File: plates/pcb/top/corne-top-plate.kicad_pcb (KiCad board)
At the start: 2 copper layers, 132.9 x 91.4 mm, 28 parts, among them SW2 KEY_SWITCH

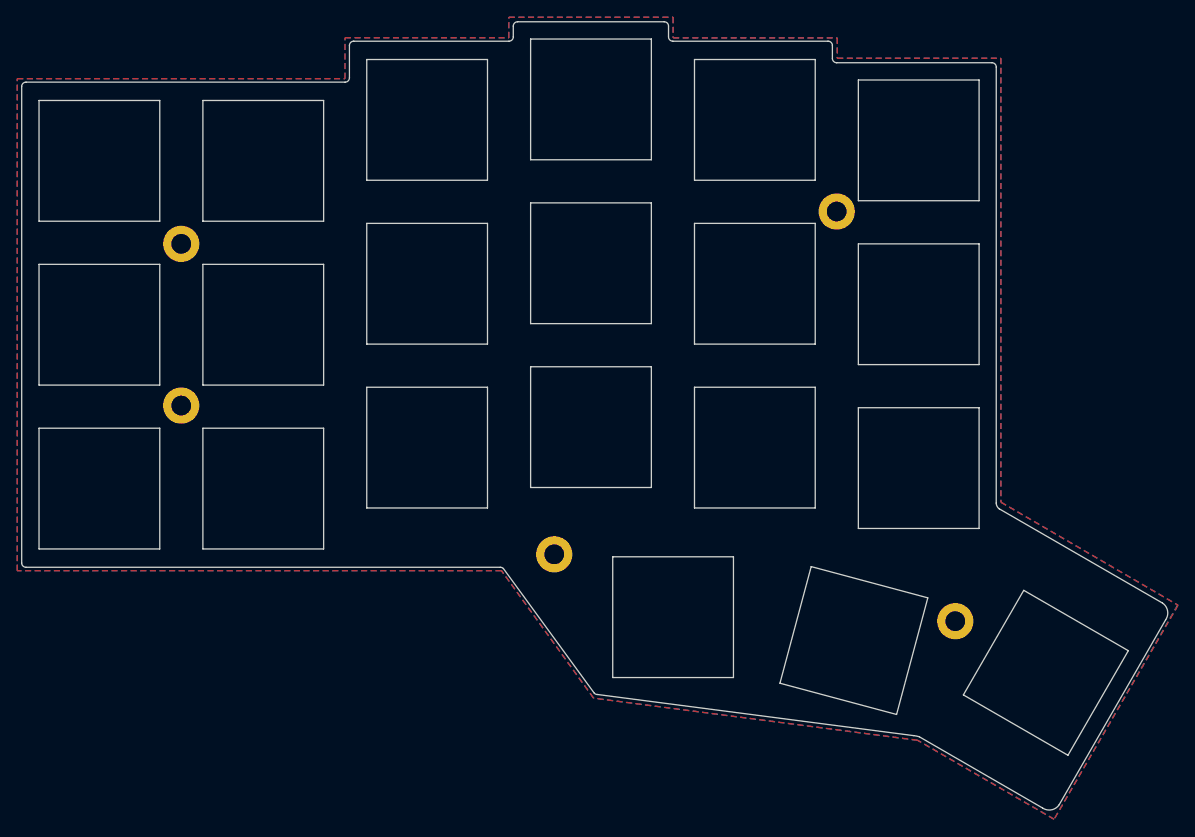
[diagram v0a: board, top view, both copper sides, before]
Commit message: Added light ice trackball inital design.
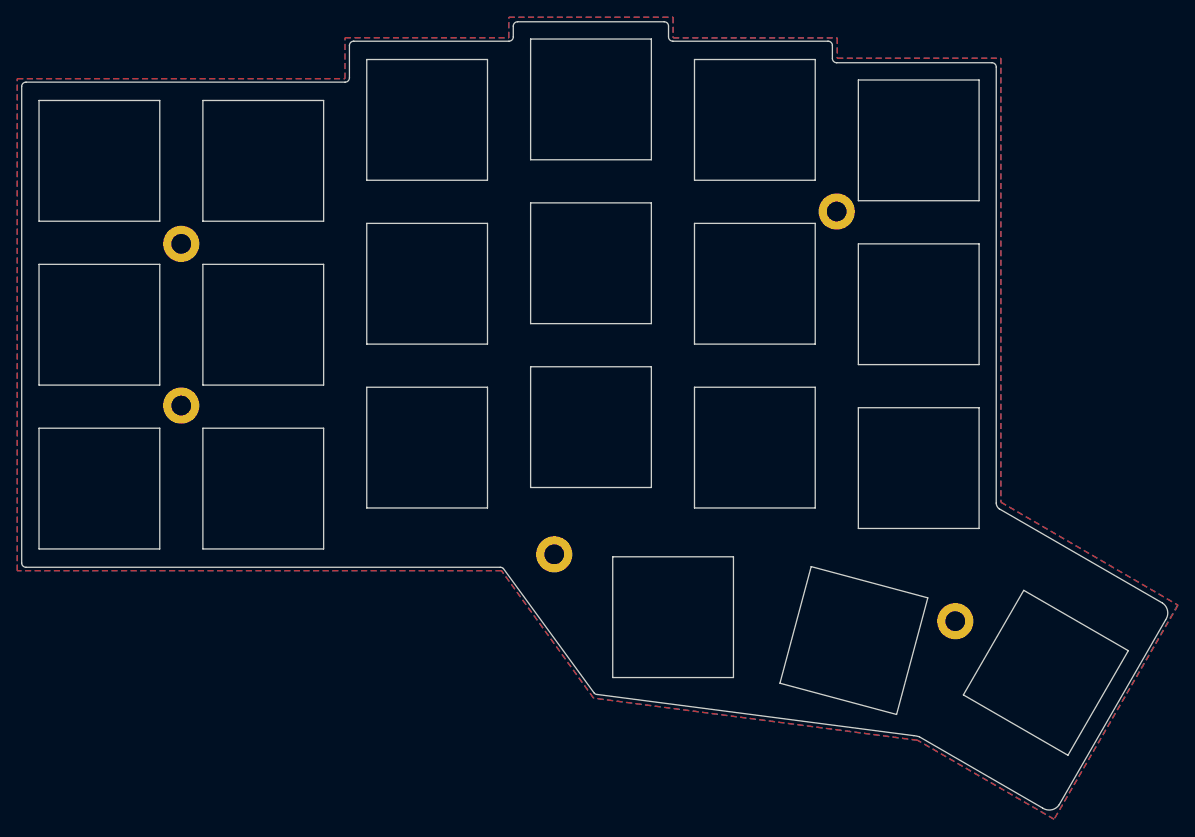
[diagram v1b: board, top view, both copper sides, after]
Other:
- net class Default removed
